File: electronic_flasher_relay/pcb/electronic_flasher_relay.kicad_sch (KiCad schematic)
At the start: 12 parts, among them J1 Conn_01x03, Q1 PN2222A, Q2 IRF5210, U1 NE555P

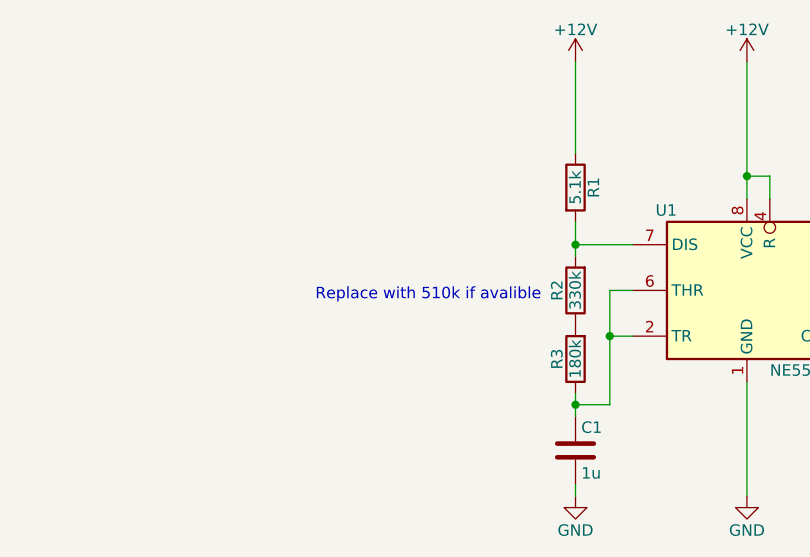
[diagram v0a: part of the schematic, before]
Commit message: change resistor values
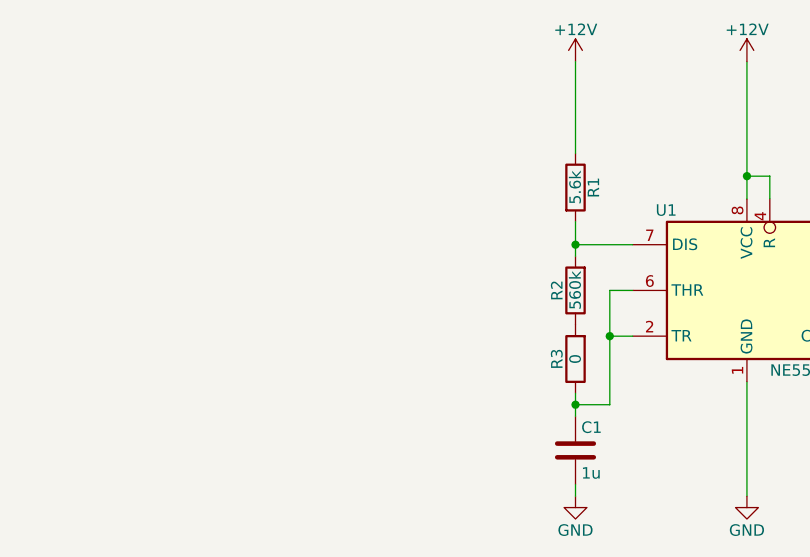
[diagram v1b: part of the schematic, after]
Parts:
- R1: value 5.1k -> 5.6k
- R2: value 330k -> 560k
- R3: value 180k -> 0
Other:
- note removed: "Replace with 510k if avalible"
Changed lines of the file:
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@@
     (effects (font (size 1.27 1.27)) (justify left bottom))
-  )
-  (text "Replace with 510k if avalible" (at 88.9 91.44 180)
-    (effects (font (size 1.27 1.27)) (justify right bottom))
   )
   (label "OUT" (at 180.34 85.09 0)
@@
     (in_bom yes) (on_board yes)
     (property "Reference" "R3" (id 0) (at 90.678 97.79 90))
-    (property "Value" "180k" (id 1) (at 92.71 97.79 90))
+    (property "Value" "0" (id 1) (at 92.71 97.79 90))
     (property "Footprint" "Resistor_THT:R_Axial_DIN0207_L6.3mm_D2.5mm_P10.16mm_Horizontal" (id 2) (at 94.488 97.79 90)
       (effects (font (size 1.27 1.27)) hide)
@@
     (in_bom yes) (on_board yes)
     (property "Reference" "R2" (id 0) (at 90.678 90.17 90))
-    (property "Value" "330k" (id 1) (at 92.71 90.17 90))
+    (property "Value" "560k" (id 1) (at 92.71 90.17 90))
     (property "Footprint" "Resistor_THT:R_Axial_DIN0207_L6.3mm_D2.5mm_P10.16mm_Horizontal" (id 2) (at 94.488 90.17 90)
       (effects (font (size 1.27 1.27)) hide)
@@
     (in_bom yes) (on_board yes)
     (property "Reference" "R1" (id 0) (at 94.742 78.74 90))
-    (property "Value" "5.1k" (id 1) (at 92.71 78.74 90))
+    (property "Value" "5.6k" (id 1) (at 92.71 78.74 90))
     (property "Footprint" "Resistor_THT:R_Axial_DIN0207_L6.3mm_D2.5mm_P10.16mm_Horizontal" (id 2) (at 90.932 78.74 90)
       (effects (font (size 1.27 1.27)) hide)
@@
     )
     (path "/ab85cc0b-5297-47fc-8888-fc3611014dd5"
-      (reference "R1") (unit 1) (value "5.1k") (footprint "Resistor_THT:R_Axial_DIN0207_L6.3mm_D2.5mm_P10.16mm_Horizontal")
+      (reference "R1") (unit 1) (value "5.6k") (footprint "Resistor_THT:R_Axial_DIN0207_L6.3mm_D2.5mm_P10.16mm_Horizontal")
     )
     (path "/93b7da2b-08be-4c7e-889b-e43c95d531a4"
-      (reference "R2") (unit 1) (value "330k") (footprint "Resistor_THT:R_Axial_DIN0207_L6.3mm_D2.5mm_P10.16mm_Horizontal")
+      (reference "R2") (unit 1) (value "560k") (footprint "Resistor_THT:R_Axial_DIN0207_L6.3mm_D2.5mm_P10.16mm_Horizontal")
     )
     (path "/492390ab-f458-456c-a7d6-39365097a3be"
-      (reference "R3") (unit 1) (value "180k") (footprint "Resistor_THT:R_Axial_DIN0207_L6.3mm_D2.5mm_P10.16mm_Horizontal")
+      (reference "R3") (unit 1) (value "0") (footprint "Resistor_THT:R_Axial_DIN0207_L6.3mm_D2.5mm_P10.16mm_Horizontal")
     )
     (path "/9578b3ad-62f7-4066-a50e-8b93374bfa4a"
